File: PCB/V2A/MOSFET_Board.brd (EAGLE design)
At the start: 120 x 110 mm, 224 parts, among them J203 CTRL, Q101 BC807, Q102 BC817, Q103 BC807, Q104 BC817, Q105 BC817, Q106 BC807, Q107 BC817, Q108 BC807, Q109 SIRC10DP, Q110 SIRC10DP, Q111 BC817, Q112 BC817, Q113 SIRC10DP, Q114 SIRC10DP, Q115 BC817, Q116 BC807, Q117 BC817, Q118 BC807, Q119 IXTK102N65X2, Q120 IXTK102N65X2, Q301 BC807, Q302 BC807, Q303 BC807, Q304 BC807, Q305 BC807, Q306 BC807, Q307 BC807, Q308 BC807, Q310 BC807, Q311 BC807, Q313 BC807, Q314 BC807, U101 AD420, U102 AD420, U103 AD620, U104 AD620, U105 AD620, U106 AD620, U107 AD620, U108 AD620, U109 LTC1865_S8, U110 LTC1865_S8, U201 LP2985, U202 LP2985, U203 LP2985, U204 AD620, U208 LTC1865_S8, U301 HCPL-063N, U302 HCPL-063N, U303 HCPL-063N, U304 HCPL-063N, U306 HCPL-063N, U307 HCPL-063N

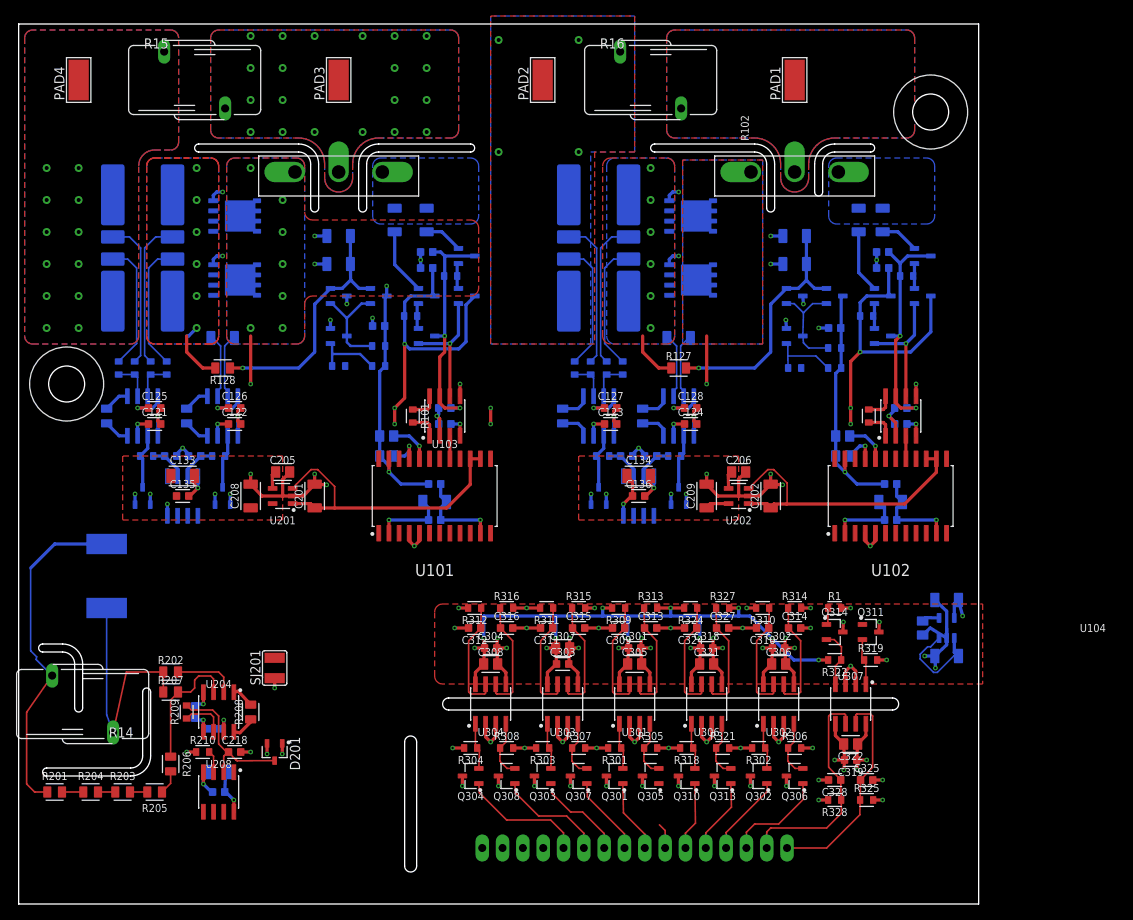
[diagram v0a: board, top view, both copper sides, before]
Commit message: V2A fully routed
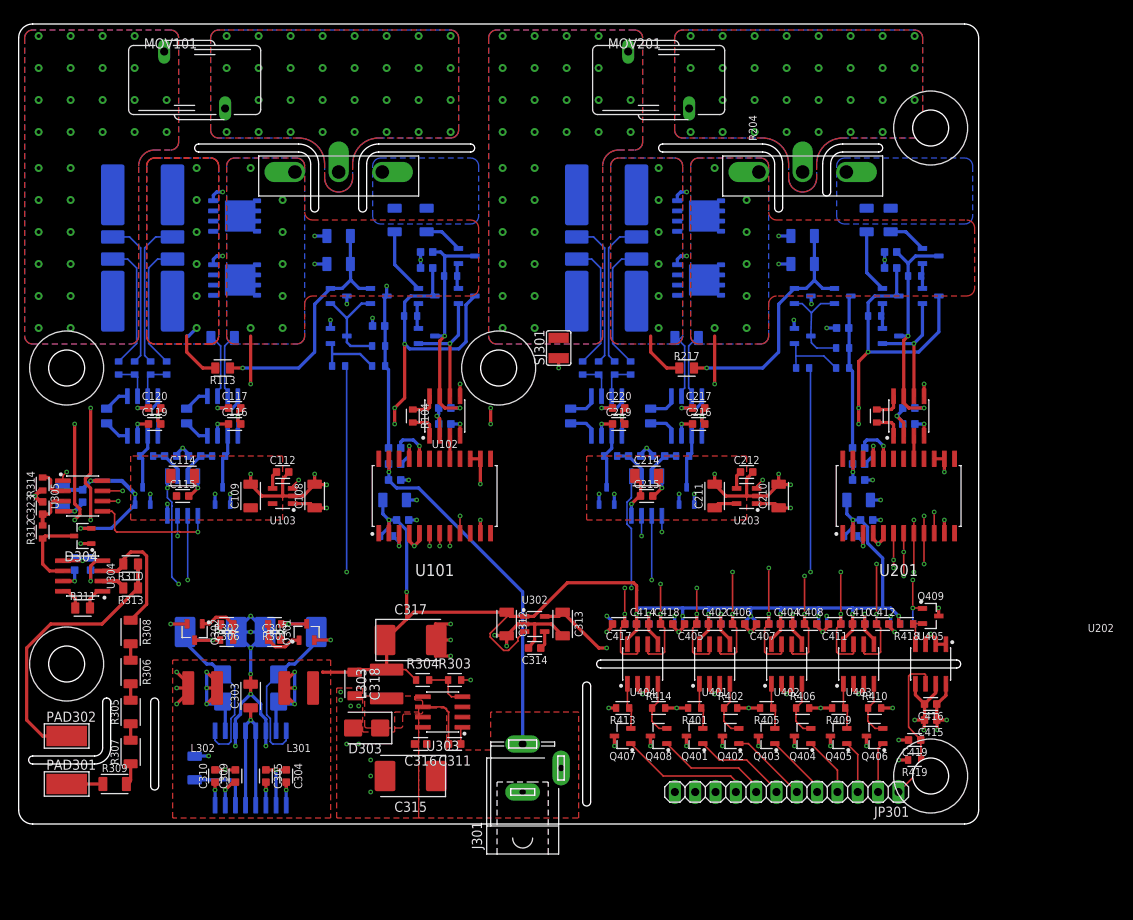
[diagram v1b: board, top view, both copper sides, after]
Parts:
- removed C122, C123, C124, C125, C126, C127, C128, C135, C136, C228: 100n, custom_capacitors:CAPC1508X45
- removed C129, C130, C131, C132: 470p, custom_capacitors:CAPC1508X45
- removed C133, C134, C224: 4µ7, custom_capacitors:CAPC3216X135
- removed C324, C325, C327, C328: 15p, custom_capacitors:CAPC1508X45
- removed D103, D104: BAT54S, custom_semiconductors_discrete:SOT95P230X110-3
- removed J203: CTRL, mechanical:HEAD_MALE_1X16
- removed PAD1, PAD2, PAD3, PAD4, PAD5, PAD6: WIREPADSMD5-2,5, wirepad:5-2,5
- removed Q111, Q112, Q115, Q117: BC817, custom_semiconductors_discrete:SOT95P240X110-3
- removed Q113, Q114: SIRC10DP, custom_semiconductors_discrete:POWERPAK-SO-8
- removed Q116, Q118, Q303, Q304, Q305, Q306, Q307, Q308, Q310, Q311, Q313, Q314: BC807, custom_semiconductors_discrete:SOT95P240X110-3
- removed Q119, Q120: IXTK102N65X2, custom_semiconductors_discrete:TO-264P-V
- removed R1, R315, R316: 1k, custom_resistors:RESC1608X70
- removed R10, R11, R12, R13, R6, R7, R8, R9: 5k, custom_resistors:RESC1608X70
- removed R125: 2R, custom_resistors:RESC3216X71
- removed R127, R128, R132, R133, R134: 2k15, custom_resistors:RESC2012X65
- removed R135, R137, R138: 100R, custom_resistors:RESC1608X70
- removed R14, R16: (no value), custom_resistors:S14K680
- removed R2, R3, R4, R5: 0R003, custom_resistors:WSL3637_0.01
- removed R318, R319, R321, R322, R324, R325, R327, R328: 350R, custom_resistors:RESC1608X70
- removed SJ201: DUT_GND, jumper:SJW
- removed U$6: (no value), mechanical:M4
- removed U107, U108: AD620, custom_semiconductors:SOIC127P599X175-8
- removed U109, U110, U208: LTC1865_S8, custom_semiconductors:SOIC127P599X175-8
- removed U306, U307: HCPL-063N, custom_semiconductors:SOIC127P599X175-8
- added C204: 470n, custom_capacitors:CAPC1508X45
- added C211, C214: 4µ7, custom_capacitors:CAPC3216X135
- added C212, C402, C404, C410, C414, C416: 10n, custom_capacitors:CAPC1508X45
- added C213, C215, C217, C220, C320, C401, C403, C409, C413, C415: 100n, custom_capacitors:CAPC1508X45
- added C221, C323: 470p, custom_capacitors:CAPC1508X45
- added C317: 100µ 10V, custom_capacitors:CAPCP7343X310
- added C405, C406, C407, C408, C411, C412, C417, C418, C419: 15p, custom_capacitors:CAPC1508X45
- added D202, D304: BAT54S, custom_semiconductors_discrete:SOT95P230X110-3
- added D301, D302, D303: SK12, custom_semiconductors_discrete:DIOM4336X262
- added J301: (no value), custom_mechanical:SPC4078
- added JP301: (no value), pinhead:1X12
- added L301, L302: 100µ, custom_inductors:SRN5040
- added L303: 47µ, custom_inductors:SRN5040
- added MOV201: (no value), custom_resistors:S14K680
- added PAD301, PAD302: WIREPADSMD5-2,5, wirepad:5-2,5
- added Q201, Q203, Q208, Q209: BC817, custom_semiconductors_discrete:SOT95P240X110-3
- added Q202, Q204, Q210, Q401, Q402, Q403, Q404, Q405, Q406, Q407, Q408, Q409: BC807, custom_semiconductors_discrete:SOT95P240X110-3
- added Q205: IXTK102N65X2, custom_semiconductors_discrete:TO-264P-V
- added Q206, Q207: SIRC10DP, custom_semiconductors_discrete:POWERPAK-SO-8
- added R211, R218, R219: 5k, custom_resistors:RESC1608X70
- added R212: 100k, custom_resistors:RESC1608X70
- added R213, R216, R411, R412, R415, R416, R417: 1k, custom_resistors:RESC1608X70
- added R214, R215: 0R003, custom_resistors:WSL3637_0.01
- added R217, R220, R222: 2k15, custom_resistors:RESC2012X65
- added R221, R223: 100R, custom_resistors:RESC1608X70
- added R401, R402, R403, R404, R405, R406, R407, R408, R409, R410, R413, R414, R418, R419: 350R, custom_resistors:RESC1608X70
- added SJ301: DUT_GND, jumper:SJW
- added U$2, U$3, U$4, U$5: (no value), custom_mechanical:M4
- added U205, U305: LTC1865_S8, custom_semiconductors:SOIC127P599X175-8
- added U206: AD620, custom_semiconductors:SOIC127P599X175-8
- added U401, U402, U403, U404, U405: HCPL-063N, custom_semiconductors:SOIC127P599X175-8
- C102, C203, C208: value 4µ7 -> 100n; device custom_capacitors:CAPC3216X135 -> custom_capacitors:CAPC1508X45
- C103, C104, C112, C304: value 100n -> 10n
- C107, C306: value 10n -> 470n; device custom_capacitors:CAPC2012X110 -> custom_capacitors:CAPC1508X45
- C108, C109, C205, C308: value 10n -> 4µ7; device custom_capacitors:CAPC2012X110 -> custom_capacitors:CAPC3216X135
- C110, C206, C207, C305, C321, C322: value 10n -> 100n; device custom_capacitors:CAPC2012X110 -> custom_capacitors:CAPC1508X45
- C111, C302: value 100n -> 470n
- C114, C303, C318, C319: value 100n -> 4µ7; device custom_capacitors:CAPC1508X45 -> custom_capacitors:CAPC3216X135
- C115, C116, C117: value 470n -> 100n
- C118: value 470n -> 470p
- C121: value 100n -> 470p
- C201, C202: value 4µ7 -> 10n; device custom_capacitors:CAPC3216X135 -> custom_capacitors:CAPC1508X45
- C209: value 4µ7 -> 470n; device custom_capacitors:CAPC3216X135 -> custom_capacitors:CAPC1508X45
- C301: value 100n -> 15µ 25V; device custom_capacitors:CAPC1508X45 -> custom_capacitors:CAPCP7343X310
- C307: value 10n -> 15µ 25V; device custom_capacitors:CAPC2012X110 -> custom_capacitors:CAPCP7343X310
- C309: value 15p -> 470n
- C310, C311, C314: value 15p -> 10n
- C312, C313: value 15p -> 4µ7; device custom_capacitors:CAPC1508X45 -> custom_capacitors:CAPC3216X135
- C315: value 15p -> 15µ 25V; device custom_capacitors:CAPC1508X45 -> custom_capacitors:CAPCP7343X310
- C316: value 15p -> 100n
- MOV101: value (none) -> 680V
- Q101, Q103, Q106, Q301, Q302: value BC807 -> BC817
- Q102, Q104: value BC817 -> BC807
- Q105: value BC817 -> IXTK102N65X2; device custom_semiconductors_discrete:SOT95P240X110-3 -> custom_semiconductors_discrete:TO-264P-V
- Q107: value BC817 -> SIRC10DP; device custom_semiconductors_discrete:SOT95P240X110-3 -> custom_semiconductors_discrete:POWERPAK-SO-8
- Q108: value BC807 -> SIRC10DP; device custom_semiconductors_discrete:SOT95P240X110-3 -> custom_semiconductors_discrete:POWERPAK-SO-8
- Q109: value SIRC10DP -> BC817; device custom_semiconductors_discrete:POWERPAK-SO-8 -> custom_semiconductors_discrete:SOT95P240X110-3
- Q110: value SIRC10DP -> BC807; device custom_semiconductors_discrete:POWERPAK-SO-8 -> custom_semiconductors_discrete:SOT95P240X110-3
- R101: value 49k3 -> 5k
- R102: value 49k3 -> 2R; device custom_resistors:RESC1608X70 -> custom_resistors:RESC3216X71
- R104: value 5k -> 49k3
- R105: value 5k -> 2R; device custom_resistors:RESC1608X70 -> custom_resistors:RESC3216X71
- R107: value 2R -> 100k; device custom_resistors:RESC3216X71 -> custom_resistors:RESC1608X70
- R108: value 2R -> 1k; device custom_resistors:RESC3216X71 -> custom_resistors:RESC1608X70
- R113, R310, R311: value 1k -> 2k15; device custom_resistors:RESC1608X70 -> custom_resistors:RESC2012X65
- R114, R118: value 2R -> 5k; device custom_resistors:RESC3216X71 -> custom_resistors:RESC1608X70
- R115: value 100k -> 5k
- R116: value 100k -> 0R003; device custom_resistors:RESC1608X70 -> custom_resistors:WSL3637_0.01
- R117: value 1k -> 0R003; device custom_resistors:RESC1608X70 -> custom_resistors:WSL3637_0.01
- R119: value 1k -> 5k
- R120: value 2R -> 2k15; device custom_resistors:RESC3216X71 -> custom_resistors:RESC2012X65
- R123: value 2R -> 100R; device custom_resistors:RESC3216X71 -> custom_resistors:RESC1608X70
- R201, R206: value 2M -> 5k; device custom_resistors:RESC2012X65 -> custom_resistors:RESC1608X70
- R202: value 2k15 -> 5k; device custom_resistors:RESC2012X65 -> custom_resistors:RESC1608X70
- R203, R205: value 2M -> 2R; device custom_resistors:RESC2012X65 -> custom_resistors:RESC3216X71
- R204: value 2M -> 49k3; device custom_resistors:RESC2012X65 -> custom_resistors:RESC1608X70
- R207, R208: value 2k15 -> 2R; device custom_resistors:RESC2012X65 -> custom_resistors:RESC3216X71
- R209: value 100R -> 2R; device custom_resistors:RESC1608X70 -> custom_resistors:RESC3216X71
- R210: value 10k -> 5k
- R303, R304: value 350R -> 10k
- R305, R306, R307, R308, R309: value 350R -> 2M; device custom_resistors:RESC1608X70 -> custom_resistors:RESC3216X71
- R312: value 1k -> 100R
- R313: value 350R -> 2k15; device custom_resistors:RESC1608X70 -> custom_resistors:RESC2012X65
- R314: value 1k -> 10k
- U$1: device mechanical:M4 -> custom_mechanical:M4
- U102: value AD420 -> AD620; device custom_semiconductors:SOIC127P1032X265-24 -> custom_semiconductors:SOIC127P599X175-8
- U103: value AD620 -> LP2985; device custom_semiconductors:SOIC127P599X175-8 -> custom_semiconductors:SOT95P280X145-5
- U105: value AD620 -> LTC1865_S8
- U201: value LP2985 -> AD420; device custom_semiconductors:SOT95P280X145-5 -> custom_semiconductors:SOIC127P1032X265-24
- U202: value LP2985 -> AD620; device custom_semiconductors:SOT95P280X145-5 -> custom_semiconductors:SOIC127P599X175-8
- U301: value HCPL-063N -> MAX743; device custom_semiconductors:SOIC127P599X175-8 -> custom_semiconductors:SOIC127P1032X265-16
- U302: value HCPL-063N -> LP2985; device custom_semiconductors:SOIC127P599X175-8 -> custom_semiconductors:SOT95P280X145-5
- U303: value HCPL-063N -> LM2671M
- U304: value HCPL-063N -> AD620
- moved R201 125.4 mm to (96.0, 95.5), flipped to the bottom
- moved R203 119.7 mm to (93.0, 102.5), flipped to the bottom, turned to 270 degrees
- moved U$1 118.6 mm to (98.0, 33.0)
- moved R205 114.2 mm to (90.0, 102.5), flipped to the bottom, turned to 90 degrees
- moved R204 108.9 mm to (91.3, 78.0), turned to 270 degrees
- moved R206 104.3 mm to (91.0, 90.5), flipped to the bottom, turned to 180 degrees
- moved C319 103.9 mm to (-10.5, 68.0), flipped to the bottom, turned to 270 degrees
- moved C322 97.6 mm to (-7.00, 59.5), flipped to the bottom, turned to 90 degrees
- moved R209 97.3 mm to (82.0, 100.5), flipped to the bottom, turned to 0 degrees
- moved R314 95.3 mm to (-13.0, 69.5), turned to 90 degrees
- moved C114 90.0 mm to (4.50, 70.5), flipped to the top, turned to 0 degrees
- moved C118 89.2 mm to (6.00, 73.0), turned to 0 degrees
- moved R208 88.9 mm to (82.0, 97.0), flipped to the bottom, turned to 0 degrees
- moved R117 88.4 mm to (-0.50, 104.5)
- moved R202 86.7 mm to (88.0, 63.0), flipped to the bottom
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- renumbered R131 to R122, R136 to R121, R15 to MOV101
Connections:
- removed net CLR_DAC1: C324.1, R324.1, U101.6, U306.7
- removed net CLR_DAC1_I: J203.6, Q310.1
- removed net CLR_DAC2: C313.1, R313.1, U102.6, U301.6
- removed net CLR_DAC2_I: J203.7
- removed net CONV_TEMP: C311.1, R311.1, U303.7
- removed net CONV_TEMP_I: J203.10
- removed net FAN1_PWM_I: J203.14
- removed net FAN2_PWM_I: J203.13
- removed net FLT_DAC: Q311.1, U101.3, U102.3
- removed net FLT_DAC_I: C325.1, J203.1, R325.1, U307.7
- removed net SDO_DAC1: U101.10, U102.9
- new net CLR_DAC: C407.1, R407.1, U101.6, U201.6, U402.7
- new net CLR_DAC_I: JP301.5, Q403.1
- new net N$28: R314.2, U305.2
- new net N$55: C310.1, U301.8
- new net N$60: R103.1, U101.3
- new net N$61: C309.1, U301.7
- new net N$64: C304.2, U301.1
- new net N$65: D301.2, L301.2, U301.15
- new net N$69: D302.1, L302.1, U301.10
- new net N$70: C301.1, D301.1, Q301.3, R301.1, U301.16
- new net N$71: C302.1, Q301.1, R301.2
- new net N$72: C307.2, D302.2, Q302.3, R302.1, U301.9
- new net N$73: C306.1, Q302.1, R302.2
- new net VREF_MAX743: C308.1, U301.6
- net +12V: now also C103.1, C104.1, C113.1, C201.1, C202.1, C207.1, C213.1, C315.1, C316.1, J301.3, Q106.3, Q208.3, R107.2, R108.2, R212.2, R213.2, U201.23, U303.8; no longer C106.1, C107.1, C108.1, C109.1, C110.1, C119.1, C120.1, Q115.3, Q117.3, R115.2, R116.2, R117.2, R119.2, U102.23
- net +15V: now also C106.1, C107.1, C116.1, C119.1, C203.1, C204.1, C219.1, C321.1, Q101.3, Q103.3, Q201.3, Q203.3, Q301.2, R101.2, R201.2, U102.7, U202.7, U206.7, U304.7; no longer C111.1, C113.1, C115.1, C117.1, C121.1, C122.1, C123.1, C124.1, Q102.3, Q104.3, Q105.3, Q107.3, R103.2, R105.2, U103.7, U105.7, U107.7, U108.7
- net +3V3: now also C313.1, R411.2, R412.2, R415.2, R416.2, U302.5; no longer C210.1, R310.2, R311.2, R312.2, R314.2, R315.2, R316.2, U203.5
- net +3V_1: now also C109.1, C114.1, C115.1, C319.1, C320.1, D304.2, U103.5, U105.8, U305.8; no longer C133.1, C135.1, C208.1, U109.8, U201.5
- net +3V_2: now also C211.1, C214.1, C215.1, D202.2, U203.5, U205.8; no longer C134.1, C136.1, C209.1, C224.1, C228.1, D103.2, D104.2, U110.8, U202.5, U208.8
- net +5V: now also C205.1, C206.1, C305.2, C312.1, C317.1, C401.1, C402.1, C403.1, C404.1, C409.1, C410.1, C413.1, C414.1, L301.1, L303.2, R103.2, R202.2, R304.1, R403.2, R404.2, R407.2, R408.2, R417.2, R418.2, U201.2, U301.12, U301.13, U301.3, U301.4, U301.5, U302.1, U302.3, U401.8, U402.8, U403.8, U404.8; no longer C103.1, C104.1, C203.1, C301.1, C302.1, C304.1, C305.1, C306.1, C307.1, C308.1, C321.1, R1.2, R309.2, R313.2, R319.2, R322.2, R324.2, R327.2, U102.2, U203.1, U203.3, U301.8, U302.8, U303.8, U304.8, U306.8
- net +5V_I: now also C415.1, C416.1, JP301.12, R401.2, R402.2, R405.2, R406.2, R409.2, R410.2, R413.2, R414.2, R419.2, U405.8; no longer C319.1, C322.1, J203.16, R301.2, R302.2, R303.2, R304.2, R305.2, R306.2, R307.2, R308.2, R318.2, R321.2, R325.2, R328.2, U307.8
- net -15V: now also C110.2, C111.2, C117.1, C120.1, C208.2, C209.2, C217.1, C220.1, C322.1, Q102.3, Q104.3, Q202.3, Q204.3, Q302.2, R206.1, U102.4, U202.4, U206.4, U304.4; no longer C112.2, C114.2, C116.2, C118.2, C125.1, C126.1, C127.1, C128.1, C219.1, Q101.3, Q103.3, Q106.3, Q108.3, R104.1, U103.4, U105.4, U107.4, U108.4
- net BPY1G1: now also Q107.4, R110.2; no longer Q109.4, R112.2
- net BYP: now also C406.1, R216.1, R404.1, U401.6; no longer C309.1, R113.1, R309.1, U301.7
- net BYP1: now also Q106.2, Q110.2, R110.1, R113.1; no longer Q117.2, Q118.2, R118.1, R128.1
- net BYP1G2: now also Q108.4, R112.2; no longer Q113.4, R118.2
- net BYP2: now also Q208.2, Q210.2, R208.1, R209.1, R217.2; no longer Q115.2, Q116.2, R114.1, R120.1, R127.2
- net BYP2G1: now also Q206.4, R208.2; no longer Q110.4, R114.2
- net BYP2G2: now also Q207.4, R209.2; no longer Q114.4, R120.2
- net BYP_I: now also JP301.6, Q402.1; no longer J203.8, Q301.1
- net CONV_C1: now also C418.1, R416.1, U105.1, U404.6; no longer C315.1, R315.1, U109.1, U303.6
- net CONV_C1_I: now also JP301.8, Q408.1; no longer J203.9, Q307.1
- net CONV_C2: now also C405.1, R403.1, U205.1, U401.7; no longer C316.1, R316.1, U110.1, U304.6
- net CONV_C2_I: now also JP301.7, Q401.1; no longer J203.11, Q308.1
- net CONV_V: now also C417.1, R415.1, U305.1, U404.7; no longer C312.1, R312.1, U208.1, U304.7
- net CONV_V_I: now also JP301.9, Q407.1; no longer J203.12, Q304.1
- net CSEN_H1: now also Q107.1, Q107.2, Q107.3, Q108.1, Q108.2, Q108.3, R109.1, R113.2, R116.I1, R117.I2, U104.2; no longer Q109.1, Q109.2, Q109.3, Q113.1, Q113.2, Q113.3, R123.1, R128.2, R2.I1, R3.I2, U106.2
- net CSEN_H2: now also Q206.1, Q206.2, Q206.3, Q207.1, Q207.2, Q207.3, R207.1, R214.I1, R215.I2, R217.1, U204.2; no longer Q110.1, Q110.2, Q110.3, Q114.1, Q114.2, Q114.3, R125.1, R127.1, R4.I1, R5.I2, U108.2
- net CSEN_L1: now also Q105.3, Q107.5, Q107.6, Q107.7, Q107.8, Q108.5, Q108.6, Q108.7, Q108.8, R109.2, U102.5, U104.3; no longer Q109.5, Q109.6, Q109.7, Q109.8, Q113.5, Q113.6, Q113.7, Q113.8, Q119.3, R123.2, U103.5, U106.3
- net CSEN_L2: now also Q205.3, Q206.5, Q206.6, Q206.7, Q206.8, Q207.5, Q207.6, Q207.7, Q207.8, R207.2, U202.5, U204.3; no longer Q110.5, Q110.6, Q110.7, Q110.8, Q114.5, Q114.6, Q114.7, Q114.8, Q120.3, R125.2, U104.5, U108.3
- net DUT+: now also MOV201.2, Q105.2, Q205.2; no longer PAD1.1, PAD3.1, Q119.2, Q120.2, R16.2
- net DUT-: now also MOV201.1, R116.I2, R117.I1, R214.I2, R215.I1, SJ301.2; no longer PAD2.1, PAD4.1, R16.1, R2.I2, R3.I1, R4.I2, R5.I1, SJ201.2
- net GND: now also C107.2, C108.2, C109.2, C110.1, C111.1, C112.2, C114.2, C116.2, C118.2, C204.2, C208.1, C209.1, C211.2, C212.2, C213.2, C214.2, C215.2, C217.2, C220.2, C221.2, C304.1, C305.1, C307.1, C317.2, C319.2, C320.2, C322.2, C323.2, C401.2, C402.2, C403.2, C404.2, C405.2, C406.2, C407.2, C408.2, C409.2, C410.2, C411.2, C412.2, C413.2, C414.2, C417.2, C418.2, D202.1, D303.2, D304.1, J301.1, L302.2, Q109.2, Q110.3, Q209.2, Q210.3, Q409.3, R303.2, R314.1, SJ301.1, U102.2, U104.5, U105.4, U201.11, U201.4, U201.5, U205.4, U206.5, U301.11, U301.14, U301.2, U302.2, U303.7, U305.4, U401.5, U402.5, U403.5, U404.5, U405.1, U405.2, U405.3; no longer C103.2, C104.2, C111.2, C112.1, C114.1, C116.1, C118.1, C122.2, C123.2, C124.2, C125.2, C126.2, C127.2, C128.2, C129.2, C130.2, C131.2, C132.2, C133.2, C134.2, C135.2, C136.2, C201.2, C202.2, C208.2, C209.2, C224.2, C228.2, C304.2, C305.2, C307.2, C311.2, C324.2, C327.2, D103.1, D104.1, Q111.2, Q112.2, Q116.3, Q118.3, Q311.3, Q314.3, R210.1, SJ201.1, U102.11, U102.4, U102.5, U104.2, U105.5, U107.5, U108.5, U109.4, U110.4, U201.2, U208.4, U301.5, U302.5, U303.5, U306.5, U307.2, U307.3
- net GNDI: now also C415.2, C416.2, C419.2, JP301.10, JP301.11, Q401.3, Q402.3, Q403.3, Q404.3, Q405.3, Q406.3, Q407.3, Q408.3, U401.2, U401.3, U402.2, U402.3, U403.2, U403.3, U404.2, U404.3, U405.5, U405.7; no longer C319.2, C322.2, C325.2, C328.2, J203.15, Q301.3, Q302.3, Q303.3, Q304.3, Q305.3, Q306.3, Q307.3, Q308.3, Q310.3, Q313.3, U301.2, U301.3, U302.2, U302.3, U303.2, U303.3, U304.2, U304.3, U306.2, U306.3, U307.5
- net HIGHC1: now also C121.1, R123.2, U105.2; no longer C129.1, R135.2, U109.2
- net HIGHC2: now also C221.1, R223.2, U205.2; no longer C131.1, R137.2, U110.2
- net LATCH_DAC: now also C408.1, R408.1, U201.7, U402.6; no longer C327.1, R327.1, U102.7, U306.6
- net LATCH_DAC_I: now also JP301.4, Q404.1; no longer J203.5, Q313.1
- net LGATE_1: now also Q105.1, R102.1, R105.2; no longer Q119.1, R107.1, R108.2
- net LGATE_2: now also Q205.1, R203.1, R205.2; no longer Q120.1, R109.1, R110.2
- net LOWC1: now also C118.1, U105.3; no longer C130.1, U109.3
- net LOWC2: now also C218.1, R221.2, U205.3; no longer C132.1, R138.2, U110.3
- net MISO: now also Q409.1, R417.1, U105.6, U205.6, U305.6; no longer Q314.1, R1.1, U109.6, U110.6, U208.6
- net MISO_I: now also C419.1, JP301.1, R419.1, U405.6; no longer C328.1, J203.2, R328.1, U307.6
- net MOSI: now also C412.1, R412.1, U105.5, U201.9, U205.5, U305.5, U403.6; no longer C310.1, R310.1, U101.9, U109.5, U110.5, U208.5, U302.7
- net MOSI_I: now also JP301.2, Q406.1; no longer J203.4, Q302.1
- net N$1: now also Q101.1, Q102.2, R101.1; no longer Q101.2, Q105.1, R103.1
- net N$10: now also C112.1, U103.4; no longer C205.1, U201.4
- net N$11: now also Q104.2, R105.1; no longer Q106.2, R108.1
- net N$12: now also Q201.1, Q202.2, R201.1; no longer Q103.2, Q107.1, R105.1
- net N$13: now also Q101.2, R102.2; no longer Q105.2, R107.2
- net N$14: now also Q204.2, R205.1; no longer Q108.2, R110.1
- net N$15: now also Q201.2, R203.2; no longer Q107.2, R109.2
- net N$16: now also D101.3, U104.6; no longer D102.3, U106.6
- net N$17: now also C311.1, U303.1; no longer Q311.2, R319.1, U307.1
- net N$18: now also Q409.2, R418.1, U405.4; no longer Q314.2, R322.1, U307.4
- net N$19: now also C311.2, D303.1, L303.1, U303.6; no longer Q304.2, R304.1, U304.1
- net N$2: now also R104.2, U102.1; no longer R101.2, U103.1
- net N$20: now also R303.1, R304.2, U303.4; no longer Q308.2, R308.1, U304.4
- net N$21: now also Q405.2, R409.1, U403.1; no longer Q302.2, R302.1, U302.1
- net N$22: now also Q406.2, R410.1, U403.4; no longer Q306.2, R306.1, U302.4
- net N$23: now also D304.3, R312.1, U304.6; no longer R209.1, U204.6
- net N$24: now also R306.1, R308.2; no longer R205.1, R206.2
- net N$25: now also Q208.1, Q209.3, Q210.1, R213.1; no longer Q111.3, Q115.1, Q116.1, R117.1
- net N$26: now also R305.2, R306.2; no longer R203.2, R205.2
- net N$27: now also R305.1, R307.2; no longer R203.1, R204.2
- net N$29: now also R308.1, R310.2, U304.3; no longer R206.1, R207.2, U204.3
- net N$3: now also C103.2; no longer C107.2
- net N$30: now also C323.1, R312.2, U305.3; no longer C218.1, D201.3, R209.2, U208.2
- net N$31: now also Q209.1, R212.1, R216.2; no longer Q111.1, R111.2, R115.1
- net N$32: now also R115.2, R117.E2; no longer R3.E2, R7.2
- net N$33: now also R307.1, R309.2; no longer R201.2, R204.1
- net N$34: now also R114.1, R115.1, U106.3; no longer R6.1, R7.1, U105.3
- net N$35: now also R116.E2, R118.1; no longer R2.E2, R8.1
- net N$36: now also R313.2, U304.2; no longer R202.2, U204.2
- net N$37: now also R118.2, R119.2, U106.2; no longer R8.2, R9.2, U105.2
- net N$38: now also R117.E1, R119.1; no longer R3.E1, R9.1
- net N$39: now also R210.1, R214.E1; no longer R10.1, R4.E1
- net N$4: now also C104.2; no longer C109.2
- net N$40: now also R114.2, R116.E1; no longer R2.E1, R6.2
- net N$41: now also C201.2, U201.21; no longer C108.2, U102.21
- net N$42: now also C202.2, U201.20; no longer C110.2, U102.20
- net N$43: now also Q202.1, Q203.1, U202.6; no longer Q103.1, Q104.1, U104.6
- net N$44: now also Q203.2, Q204.1, R206.2; no longer Q104.2, Q108.1, R106.2
- net N$45: now also R202.1, U201.3; no longer R210.2, U208.3
- net N$46: now also R211.1, R215.E2; no longer R11.1, R5.E2
- net N$47: now also Q401.2, R401.1, U401.1; no longer Q301.2, R301.1, U301.1
- net N$48: now also Q402.2, R402.1, U401.4; no longer Q305.2, R305.1, U301.4
- net N$49: now also R204.2, U202.1; no longer R102.2, U104.1
- net N$5: now also Q106.1, Q109.3, Q110.1, R108.1; no longer Q112.3, Q117.1, Q118.1, R119.1
- net N$50: now also R204.1, U202.8; no longer R102.1, U104.8
- net N$51: now also U201.17, U202.3; no longer U102.17, U104.3
- net N$52: now also R215.E1, R218.2; no longer R12.2, R5.E1
- net N$53: now also R214.E2, R219.2; no longer R13.2, R4.E2
- net N$54: now also R210.2, R211.2, U206.3; no longer R10.2, R11.2, U107.3
- net N$56: now also D202.3, R223.1, U206.6; no longer D103.3, R137.1, U107.6
- net N$57: now also D201.3, R221.1, U204.6; no longer D104.3, R138.1, U108.6
- net N$58: now also Q403.2, R405.1, U402.1; no longer Q310.2, R318.1, U306.1
- net N$59: now also Q404.2, R406.1, U402.4; no longer Q313.2, R321.1, U306.4
- net N$6: now also R104.1, U102.8; no longer R101.1, U103.8
- net N$62: now also C212.1, U203.4; no longer C206.1, U202.4
- net N$63: now also R218.1, R219.1, U206.2; no longer R12.1, R13.1, U107.2
- net N$66: now also C314.1, U302.4; no longer C207.1, U203.4
- net N$67: now also Q103.1, U102.6; no longer Q101.1, U103.6
- net N$68: now also Q103.2, Q104.1, R106.2; no longer Q102.2, Q106.1, R104.2
- net N$7: now also D102.3, R123.1, U106.6; no longer D101.3, R135.1, U105.6
- net N$76: now also Q407.2, R413.1, U404.1; no longer Q303.2, R303.1, U303.1
- net N$77: now also Q408.2, R414.1, U404.4; no longer Q307.2, R307.1, U303.4
- net N$8: now also Q109.1, R107.1, R111.2; no longer Q112.1, R113.2, R116.1
- net N$9: now also U102.3; no longer U103.3
- net RG1_H6: now also R311.2, U304.1; no longer R208.2, U204.1
- net RG1_L1: now also R222.2, U206.1; no longer R133.2, U107.1
- net RG1_L2: now also R220.2, U204.1; no longer R134.2, U108.1
- net RG1_L3: now also U106.1; no longer U105.1
- net RG1_L4: now also R120.2, U104.1; no longer R132.2, U106.1
- net RG2_H6: now also R311.1, U304.8; no longer R208.1, U204.8
- net RG2_L1: now also R222.1, U206.8; no longer R133.1, U107.8
- net RG2_L2: now also R220.1, U204.8; no longer R134.1, U108.8
- net RG2_L3: now also U106.8; no longer U105.8
- net RG2_L4: now also R120.1, U104.8; no longer R132.1, U106.8
- net SCK: now also C411.1, R411.1, U105.7, U201.8, U205.7, U305.7, U403.7; no longer C314.1, R314.1, U102.8, U109.7, U110.7, U208.7, U302.6
- net SCK_I: now also JP301.3, Q405.1; no longer J203.3, Q306.1
- net SDO_DAC2: now also U101.9, U201.10; no longer U102.10
- net VREF1: now also C108.1, U103.1, U103.3; no longer C201.1, U201.1, U201.3
- net VREF2: now also C210.1, U201.14, U201.15, U203.1, U203.3; no longer C202.1, U102.14, U102.15, U202.1, U202.3
- net VSENSE+: now also PAD301.1, R309.1; no longer PAD5.1, R14.2, R201.1
- net VSENSE-: now also PAD302.1, R310.1, R313.1; no longer PAD6.1, R14.1, R202.1, R207.1
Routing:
- net SCK: track 14.5 -> 146.1 mm, vias 0 -> 8
- net MISO: track 2.11 -> 133.6 mm, vias 0 -> 5
- net MOSI: track 14.5 -> 137.7 mm, vias 0 -> 6
- net BYP: track 14.5 -> 124.2 mm, vias 0 -> 4
- net CLR_DAC: track 0.00 -> 95.6 mm, vias 0 -> 5
- net +12V: track 61.4 -> 151.2 mm
- net LATCH_DAC: track 14.5 -> 92.0 mm, vias 0 -> 5
- net CONV_V: track 14.5 -> 91.2 mm, vias 0 -> 3
- net CONV_C1: track 14.5 -> 87.7 mm, vias 0 -> 4
- net +15V: track 173.5 -> 240.2 mm, vias 11 -> 14
- net +5V: track 135.6 -> 200.0 mm, vias 18 -> 13
- net SDO_DAC2: track 0.00 -> 64.3 mm, vias 0 -> 2
- net -15V: track 202.0 -> 247.5 mm, vias 13 -> 16
- net VSENSE+: track 42.9 -> 4.53 mm
- net GND: track 215.5 -> 246.5 mm, vias 59 -> 84
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- added copper zone on layer 1, net +12V
- added copper zone on layer 1, net GND
- added copper zone on layer 15, net GNDI
- added copper zone on layer 1, net N$19
- added copper zone on layer 2, net VREF1
- added copper zone on layer 2, net VREF2
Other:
- board size 120 x 110 mm -> 120 x 100 mm
- board text removed: "+5V"
- board text removed: "->"
- board text removed: "<-"
- board text removed: "BYP"
- board text removed: "CLR1"
- board text removed: "CLR2"
- board text removed: "C_C1"
- board text removed: "C_C2"
- board text removed: "C_TEMP"
- board text removed: "C_V"
- board text removed: "FAN1"
- board text removed: "FAN2"
- board text removed: "FLT"
- board text removed: "GND"
- board text removed: "LATCH"
- board text removed: "MISO"
- board text removed: "MOSI"
- board text removed: "SCK"
